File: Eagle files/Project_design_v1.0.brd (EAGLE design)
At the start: 100 x 80 mm, 49 parts, among them CN1 USB, CN2 BATT_IN_JST, CN3 LOAD_JST, IC3 TPS73250DBVT, IC4 TPS73233DBVT, U1 MCP9700T-E/TT, U2 MCP73833T-AMI/MF

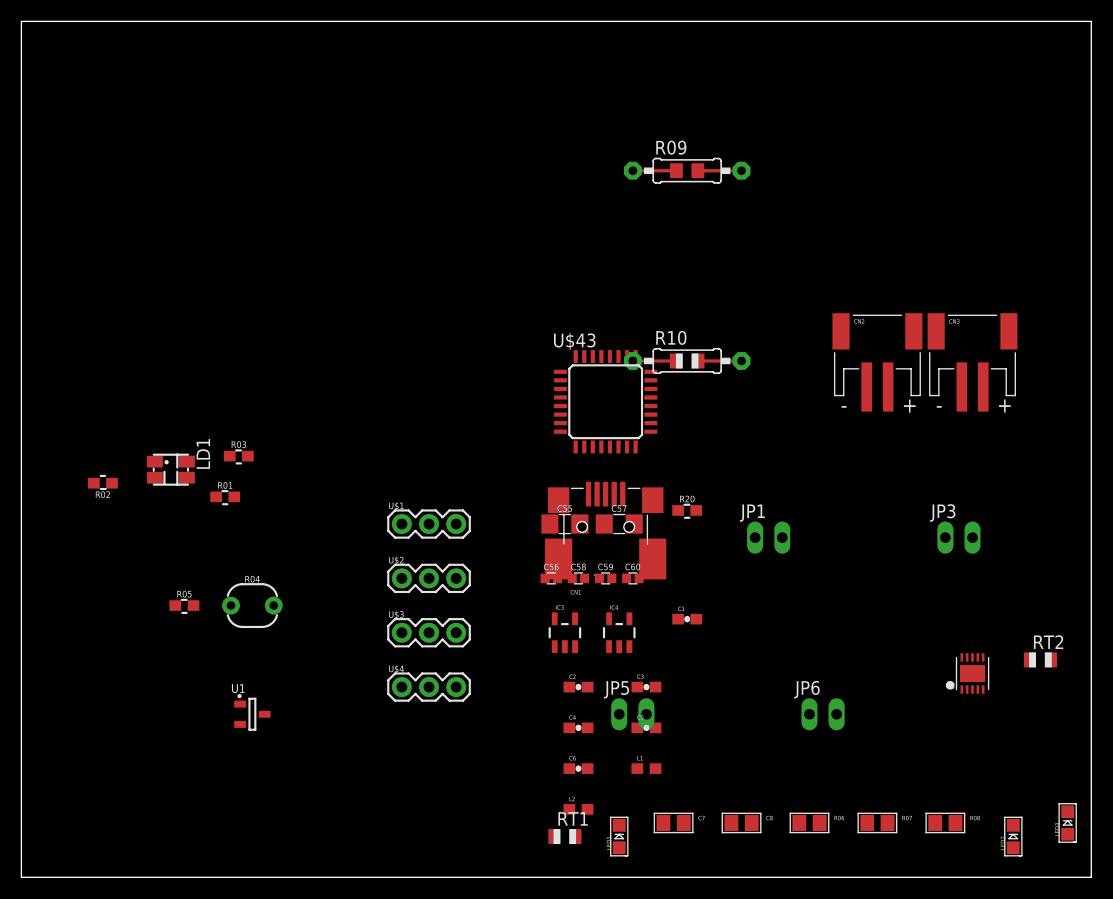
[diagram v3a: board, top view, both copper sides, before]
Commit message: corrections of few wire in the schematics
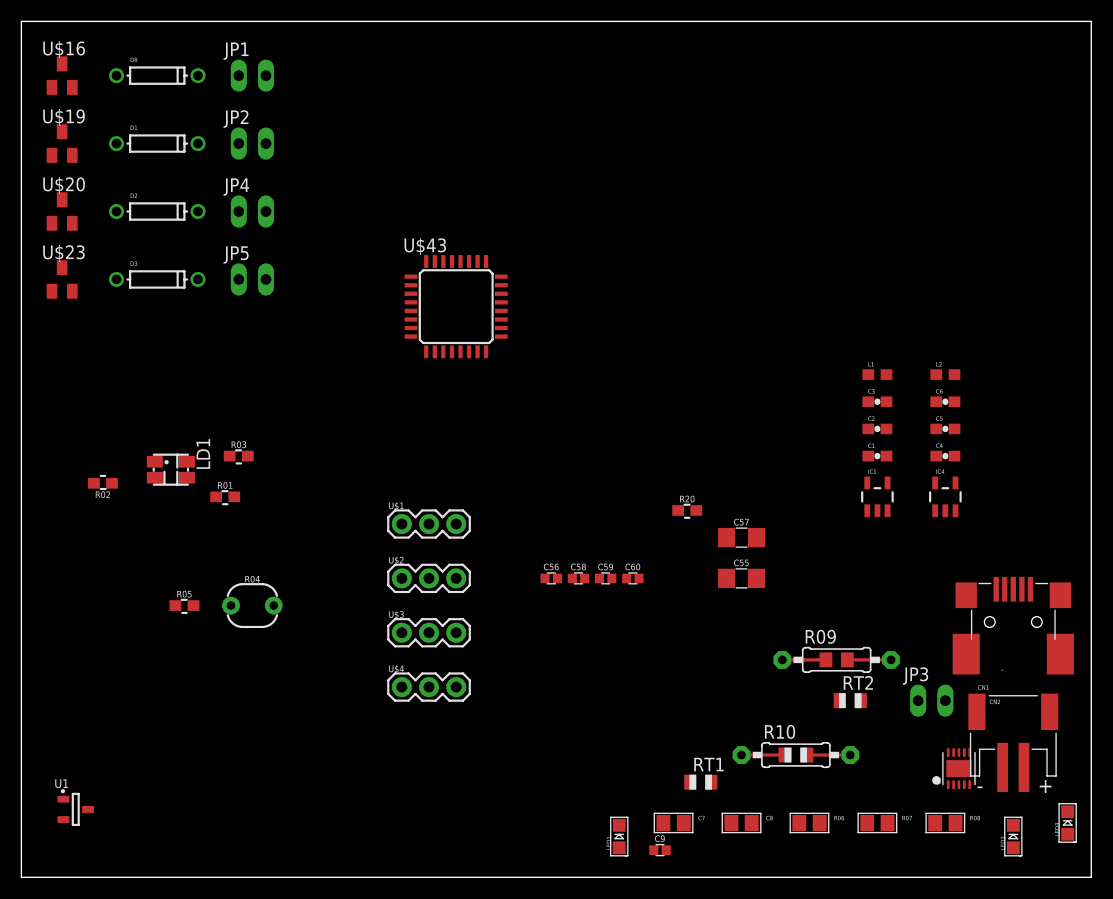
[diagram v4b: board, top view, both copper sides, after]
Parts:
- removed CN3: LOAD_JST, microbuilder:JSTPH2
- removed IC3: TPS73250DBVT, TPS32xx:SOT23-5
- removed JP6: STAT, microbuilder:1X02_OVAL
- added C9: 100n, custom_part:0402
- added D1, D2, D3, D8: (no value), adafruit:DO-1N4148
- added IC1: TPS73233DBVT, TPS32xx:SOT23-5
- added JP2: MOTOR2, microbuilder:1X02_OVAL
- added JP4: MOTOR3, microbuilder:1X02_OVAL
- added U$16, U$19, U$20, U$23: PMV16XN, custom_part_2:SOT23
- JP1: value PWR_IN_0.1 -> MOTOR1
- JP5: value BATT_IN_0.1 -> MOTOR4
- moved JP1 64.8 mm to (21.6, 74.9)
- moved JP5 54.0 mm to (21.6, 55.9)
- moved L2 53.2 mm to (86.4, 47.0)
- moved C6 48.5 mm to (86.4, 44.5)
- moved R09 47.8 mm to (76.2, 20.3)
- moved L1 42.7 mm to (80.0, 47.0)
- moved C4 42.7 mm to (86.4, 39.4)
- moved C5 39.5 mm to (86.4, 41.9)
- moved CN1 39.1 mm to (92.7, 22.9)
- moved R10 38.2 mm to (72.4, 11.4)
- moved CN2 37.8 mm to (92.7, 14.0)
- moved C2 36.9 mm to (80.0, 41.9)
- moved C3 34.3 mm to (80.0, 44.5)
- moved IC4 33.0 mm to (86.4, 35.6)
- moved C1 23.4 mm to (80.0, 39.4)
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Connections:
- removed net 5V: IC3.1, IC3.3, IC4.1, IC4.3
- removed net AVDD: C3.1, C60.1, L1.2, U$43.5
- removed net BATT: C8.1, CN2.2, CN3.2, JP3.2, JP5.2, U2.P$10, U2.P$9
- removed net DVDD: C6.1, L2.2
- new net CTRL_MOIST1: U$1.1
- new net CTRL_MOIST2: U$2.1
- new net CTRL_MOIST3: U$3.1
- new net CTRL_MOIST4: U$4.1
- new net CTRL_MOTOR1: U$16.1
- new net CTRL_MOTOR2: U$19.1
- new net CTRL_MOTOR3: U$20.1
- new net CTRL_MOTOR4: U$23.1
- new net CTRL_PHOTOCELL: R04.2
- new net N$10: D8.A, JP1.2, U$16.3
- new net N$11: D1.A, JP2.2, U$19.3
- new net N$14: D2.A, JP4.2, U$20.3
- new net N$15: D3.A, JP5.2, U$23.3
- new net VCC: C3.1, C60.1, D1.C, D2.C, D3.C, D8.C, JP1.1, JP2.1, JP4.1, JP5.1, L1.2, U$43.5
- new net V_BAT: C8.1, CN2.2, IC1.1, IC1.3, IC4.1, IC4.3, JP3.2, U2.P$10, U2.P$9
- net 3.3V: now also C6.1, L2.2; no longer R04.2, U$1.1, U$2.1, U$3.1, U$4.1
- net 5.0V: now also C9.1; no longer JP1.2
- net AGND: now also IC1.2; no longer IC3.2
- net GND: now also C9.2, U$16.2, U$19.2, U$20.2, U$23.2; no longer CN3.1, JP1.1, JP5.1
- net N$13: now also IC1.5; no longer IC3.5
- net N$5: no longer JP6.1
- net N$6: no longer JP6.2

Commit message: part number & potentiometer to select the ammount of water needed for each pot
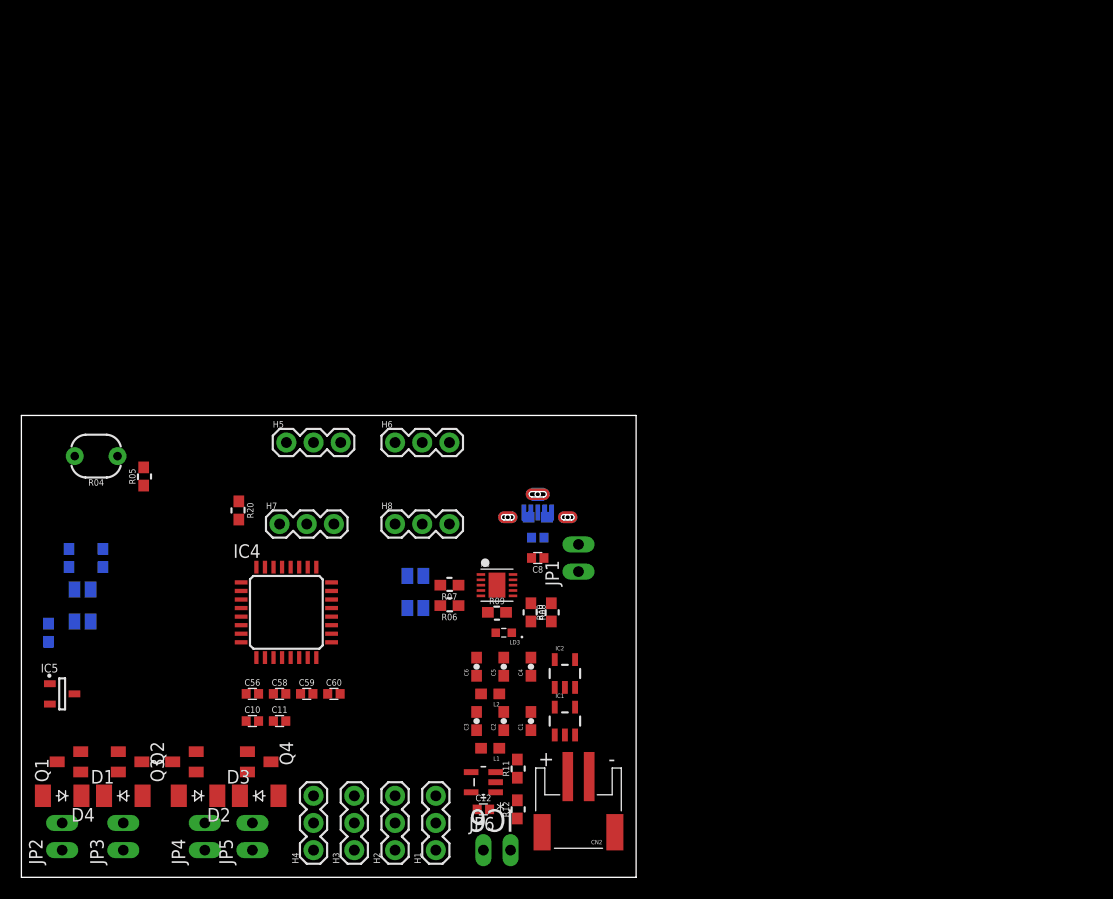
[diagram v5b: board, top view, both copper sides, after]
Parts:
- removed C55, C57: 10uF, custom_part:1206
- removed D8: (no value), adafruit:DO-1N4148
- removed LED1: STAT1-ORANGE, microbuilder:CHIPLED_0805
- removed LED2: STAT2-GREEN, microbuilder:CHIPLED_0805
- removed LED3: Power-RED, microbuilder:CHIPLED_0805
- removed RT1: 1K, adafruit:R0805
- removed RT2: 150K, adafruit:R0805
- removed U$1, U$2, U$3, U$4: SOIL_MOISTURE, potentiometer:SOIL_MOISTURE
- removed U$16, U$19, U$20, U$23: PMV16XN, custom_part_2:SOT23
- removed U$43: STM32F042K6T6, stm32-microcontrollers:LQFP32-7X7
- removed U1: MCP9700T-E/TT, MCP9700T-E_TT:SOT95P237X112-3N
- removed U2: MCP73833T-AMI/MF, microbuilder:DFN10_3X3MM
- added C10, C11, C12: 100n, custom_part:0402
- added D4: 1N4148W, diode:SOD-123_MINI-SMA
- added H1, H2, H3, H4, H5, H6, H7, H8: SOIL_MOISTURE, potentiometer:SOIL_MOISTURE
- added IC2: TPS73233DBVT, TPS32xx:SOT23-5
- added IC3: MCP73833T-AMI/MF, microbuilder:DFN10_3X3MM
- added IC5: MCP9700T-E/TT, MCP9700T-E_TT:SOT95P237X112-3N
- added IC6: TLV379IDBVT, AD8009JRTZ-REEL:SOT95P280X145-5N
- added JP6: Contact_pin, microbuilder:1X02_OVAL
- added LD2: RGB_LED, Semicond:PLCC-4
- added LD3: RLED, LTST-C190KRKT:LEDM1608X80
- added Q1, Q2, Q3, Q4: PMV16XN, custom_part_2:SOT23
- added R11, R12: 221, custom_part:0603
- C7: device microbuilder:0805 -> SparkFun-Passives:0603-CAP
- C8: value 10uF -> 100n; device microbuilder:0805 -> custom_part:0402
- CN1: value USB -> USB_CONN; device microbuilder:USB-MINIB_LARGER -> 105133-0011:MOLEX_105133-0011
- D1, D2, D3: value (none) -> 1N4148W; device adafruit:DO-1N4148 -> diode:SOD-123_MINI-SMA
- IC4: value TPS73233DBVT -> STM32F042K6T6; device TPS32xx:SOT23-5 -> stm32-microcontrollers:LQFP32-7X7
- JP1: value MOTOR1 -> Contact_pin
- JP2: value MOTOR2 -> Contact_pin
- JP3: value LOAD_0.1 -> Contact_pin
- JP4: value MOTOR3 -> Contact_pin
- JP5: value MOTOR4 -> Contact_pin
- LD1: value ASMB-MTB0-0A3A2PLCC-4 -> RGB_LED
- R01: value 3K -> 2k
- R02, R03: value 2K -> 2k
- R05, R20: value 10K -> 10k
- R06, R07, R08: value 150 -> 221; device microbuilder:0805 -> custom_part:0603
- R09: value PROG -> 2k; device microbuilder:0805-THM -> custom_part:0603
- R10: value 10K/THERM -> 10k; device adafruit:0805-THM -> custom_part:0603
- moved JP3 76.6 mm to (9.53, 3.81), turned to 90 degrees
- moved JP2 67.2 mm to (3.81, 3.81), turned to 90 degrees
- moved IC4 62.5 mm to (24.8, 24.8)
- moved D1 61.0 mm to (9.53, 7.62)
- moved JP4 58.6 mm to (17.1, 3.81), turned to 90 degrees
- moved D2 54.7 mm to (16.5, 7.62), turned to 180 degrees
- moved JP1 54.4 mm to (52.1, 29.8), turned to 90 degrees
- moved JP5 52.1 mm to (21.6, 3.81), turned to 90 degrees
- moved L2 52.0 mm to (43.8, 17.1), turned to 180 degrees
- moved C6 50.3 mm to (42.5, 19.7), turned to 90 degrees
- moved L1 50.3 mm to (43.8, 12.1), turned to 180 degrees
- moved D3 49.2 mm to (22.2, 7.62)
- moved C3 47.9 mm to (42.5, 14.6), turned to 90 degrees
- moved C5 46.9 mm to (45.1, 19.7), turned to 90 degrees
- moved R07 45.8 mm to (40.0, 27.3), turned to 180 degrees
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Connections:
- removed net AGND: C1.2, C2.2, C3.2, C4.2, C5.2, C6.2, IC1.2, IC4.2
- removed net N$9: R10.2, RT1.2, RT2.2
- new net LEVEL_SENSOR: JP6.1
- new net N$17: IC6.3, R11.1, R12.2
- new net V_BAT_SENSE: IC6.1, IC6.4
- new net WATER_ADJ_1: H5.3
- new net WATER_ADJ_2: H6.3
- new net WATER_ADJ_3: H7.3
- new net WATER_ADJ_4: H8.3
- net 3.3V: now also C10.1, C11.1, C12.1, H5.1, H6.1, H7.1, H8.1, IC4.1, IC4.17, IC5.1, IC6.5; no longer C55.1, C57.1, U$43.1, U$43.17, U1.1
- net 5.0V: now also CN1.1, IC3.P$1, IC3.P$2, LD2.1, LD3.A; no longer CN1.VBUS, LED1.A, LED2.A, LED3.A, U2.P$1, U2.P$2
- net BOOT0: now also IC4.31; no longer U$43.31
- net CHARGE_CMD: now also IC4.11; no longer U$43.11
- net CTRL_MOIST1: now also H1.1; no longer U$1.1
- net CTRL_MOIST2: now also H2.1; no longer U$2.1
- net CTRL_MOIST3: now also H3.1; no longer U$3.1
- net CTRL_MOIST4: now also H4.1; no longer U$4.1
- net CTRL_MOTOR1: now also Q1.1; no longer U$16.1
- net CTRL_MOTOR2: now also Q2.1; no longer U$19.1
- net CTRL_MOTOR3: now also Q3.1; no longer U$20.1
- net CTRL_MOTOR4: now also Q4.1; no longer U$23.1
- net DAC_CLK: now also IC4.12; no longer U$43.12
- net DAC_D2: now also IC4.13; no longer U$43.13
- net DAC_D3: now also IC4.18; no longer U$43.18
- net DAC_D4: now also IC4.19; no longer U$43.19
- net DAC_D5: now also IC4.20; no longer U$43.20
- net DAC_D6: now also IC4.21; no longer U$43.21
- net DAC_D7: now also IC4.22; no longer U$43.22
- net DAC_D8: now also IC4.25; no longer U$43.25
- net GND: now also C1.2, C10.2, C11.2, C12.2, C2.2, C3.2, C4.2, C5.2, C6.2, CN1.5, CN1.6, CN1.7, CN1.8, H1.2, H2.2, H3.2, H4.2, H5.2, H6.2, H7.2, H8.2, IC1.2, IC2.2, IC3.P$5, IC4.16, IC4.32, IC5.3, IC6.2, JP1.1, JP6.2, Q1.2, Q2.2, Q3.2, Q4.2, R12.1; no longer C55.2, C57.2, CN1.GND, JP3.1, RT2.1, U$1.2, U$16.2, U$19.2, U$2.2, U$20.2, U$23.2, U$3.2, U$4.2, U$43.16, U$43.32, U1.3, U2.P$5
- net HV_DONE: now also IC4.10; no longer U$43.10
- net LED_G: now also IC4.3; no longer U$43.3
- net LI_PRESET: now also IC4.2; no longer U$43.2
- net LOAD_CURRENT_1: now also IC4.6; no longer U$43.6
- net LOAD_CURRENT_2: now also IC4.7; no longer U$43.7
- net LOAD_CURRENT_3: now also IC4.8; no longer U$43.8
- net LOAD_CURRENT_4: now also IC4.9; no longer U$43.9
- net MOISTURE1: now also H1.3; no longer U$1.3
- net MOISTURE2: now also H2.3; no longer U$2.3
- net MOISTURE3: now also H3.3; no longer U$3.3
- net MOISTURE4: now also H4.3; no longer U$4.3
- net MUX_DIS: now also IC4.28; no longer U$43.28
- net MUX_IN: now also IC4.14; no longer U$43.14
- net MUX_S0: now also IC4.15; no longer U$43.15
- net MUX_S1: now also IC4.26; no longer U$43.26
- net MUX_S2: now also IC4.27; no longer U$43.27
- net N$10: now also D4.A, JP2.2, Q1.3; no longer D8.A, JP1.2, U$16.3
- net N$11: now also JP3.2, Q2.3; no longer JP2.2, U$19.3
- net N$12: now also LD3.C, R08.2; no longer LED3.C, R08.1
- net N$14: now also Q3.3; no longer U$20.3
- net N$15: now also Q4.3; no longer U$23.3
- net N$16: now also IC3.P$6; no longer U2.P$6
- net N$2: now also IC2.5; no longer IC4.5
- net N$3: now also LD2.3; no longer LED1.C
- net N$4: now also LD2.4; no longer LED2.C
- net N$5: now also IC3.P$3, R07.1; no longer R06.1, U2.P$3
- net N$6: now also IC3.P$4, R06.1; no longer R07.1, U2.P$4
- net N$7: now also IC3.P$7, R08.1; no longer R08.2, U2.P$7
- net N$8: now also IC3.P$8, R10.2; no longer RT1.1, U2.P$8
- net NRST: now also IC4.4; no longer U$43.4
- net SWCLK: now also IC4.24; no longer U$43.24
- net SWDIO: now also IC4.23; no longer U$43.23
- net TEMP_READ: now also IC5.2; no longer U1.2
- net USART1_RX/I2C1_SDA: now also IC4.30; no longer U$43.30
- net USART1_TX/I2C1_SCL: now also IC4.29; no longer U$43.29
- net VCC: now also D4.C, IC4.5, JP3.1; no longer D8.C, JP1.1, U$43.5
- net V_BAT: now also IC2.1, IC2.3, IC3.P$10, IC3.P$9, JP1.2, R11.2; no longer IC4.1, IC4.3, JP3.2, U2.P$10, U2.P$9
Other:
- board size 100 x 80 mm -> 57.5 x 43.2 mm
